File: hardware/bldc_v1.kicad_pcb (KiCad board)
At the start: 4 copper layers, 124.1 x 121.1 mm, 63 parts, among them J1 Conn_01x06, J2 1x2_ScrewTerminal_65A, J3 Screw_Terminal_01x05, J4 RJ45, J5 Screw_Terminal_01x03, M1 IPB044N15N5, M2 IPB044N15N5, M3 IPB044N15N5, M4 IPB044N15N5, M5 IPB044N15N5, M6 IPB044N15N5, M7 STM32F4-DISCOVERY, U1 AD8205, U2 AD8205

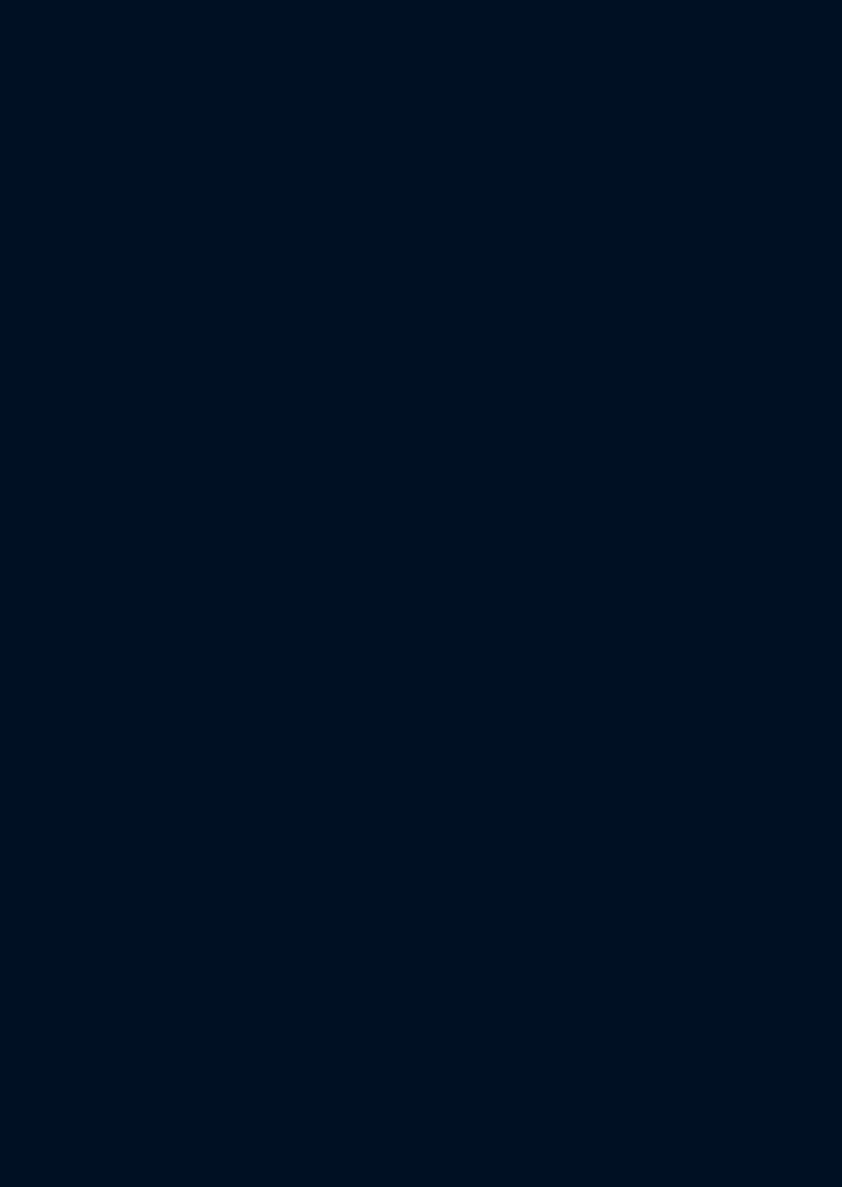
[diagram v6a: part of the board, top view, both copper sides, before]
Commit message: Added additional capacitors for 48v bus
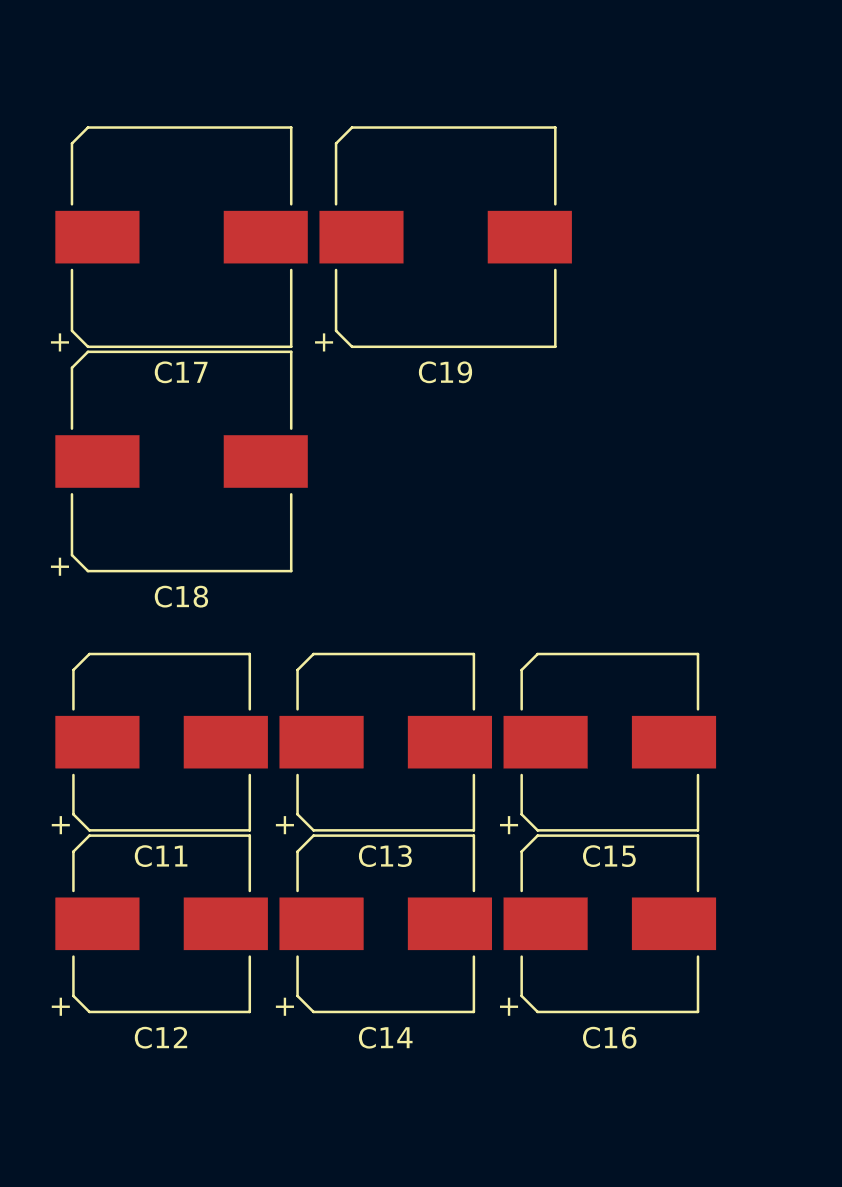
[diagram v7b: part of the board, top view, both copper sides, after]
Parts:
- added C11: 4.7u, Capacitors_SMD:CP_Elec_8x6.5, F.Cu at (40.3, 76.0)
- added C12: 4.7u, Capacitors_SMD:CP_Elec_8x6.5, F.Cu at (40.3, 84.6)
- added C13: 4.7u, Capacitors_SMD:CP_Elec_8x6.5, F.Cu at (51.0, 76.0)
- added C14: 4.7u, Capacitors_SMD:CP_Elec_8x6.5, F.Cu at (51.0, 84.6)
- added C15: 4.7u, Capacitors_SMD:CP_Elec_8x6.5, F.Cu at (61.6, 76.0)
- added C16: 4.7u, Capacitors_SMD:CP_Elec_8x6.5, F.Cu at (61.6, 84.6)
- added C17: 100u, Capacitors_SMD:CP_Elec_10x10, F.Cu at (41.3, 52.0)
- added C18: 100u, Capacitors_SMD:CP_Elec_10x10, F.Cu at (41.3, 62.7)
- added C19: 100u, Capacitors_SMD:CP_Elec_10x10, F.Cu at (53.8, 52.0)
- C1, C2, C3: value 0.1u -> 0.68u
- C4, C5, C6: value 1.0u -> 10.0u
- M1, M2, M3, M4, M5, M6: value IPB044N15N5 -> IPB017N10N5
- PhaseA1, PhaseB1, PhaseC1: value UCC2720xA -> UCC27211A
